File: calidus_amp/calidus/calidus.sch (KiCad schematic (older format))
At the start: 12 parts, among them J1 left_out, J10 service, J11 led_power, J12 sense_bus, J2 power, J3 right_out, J4 left_pot, J5 icsp, J6 input, J7 mute_key, J8 right_pot, J9 led_overload

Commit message: Updated schematic and footprinted Rybicon capacitors
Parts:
- added H1, H2, H3, H4: Mounting, MountingHole:MountingHole_3.2mm_M3_Pad, symbol Mechanical:MountingHole_Pad
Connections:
- no-connect marks 1 -> 5
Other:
- note added: "Mechanical elements"
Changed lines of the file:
@@
 	4700 5100 4700 3900
 Connection ~ 4700 3900
+$Comp
+L Graphic:Logo_Open_Hardware_Small #LOGO1
+U 1 1 5C57F80E
+P 2900 7100
+F 0 "#LOGO1" H 2900 7375 50  0001 C CNN
+F 1 "Logo_Open_Hardware_Small" H 2900 6875 50  0001 C CNN
+F 2 "" H 2900 7100 50  0001 C CNN
+F 3 "~" H 2900 7100 50  0001 C CNN
+	1    2900 7100
+	1    0    0    -1
+$EndComp
+$Comp
+L Mechanical:MountingHole_Pad H1
+U 1 1 5C57F9BC
+P 1200 6900
+F 0 "H1" H 1300 6951 50  0000 L CNN
+F 1 "Mounting" H 1300 6860 50  0000 L CNN
+F 2 "MountingHole:MountingHole_3.2mm_M3_Pad" H 1200 6900 50  0001 C CNN
+F 3 "~" H 1200 6900 50  0001 C CNN
+	1    1200 6900
+	1    0    0    -1
+$EndComp
+NoConn ~ 1200 7000
+$Comp
+L Mechanical:MountingHole_Pad H3
+U 1 1 5C581F06
+P 1200 7200
+F 0 "H3" H 1300 7251 50  0000 L CNN
+F 1 "Mounting" H 1300 7160 50  0000 L CNN
+F 2 "MountingHole:MountingHole_3.2mm_M3_Pad" H 1200 7200 50  0001 C CNN
+F 3 "~" H 1200 7200 50  0001 C CNN
+	1    1200 7200
+	1    0    0    -1
+$EndComp
+NoConn ~ 1200 7300
+$Comp
+L Mechanical:MountingHole_Pad H2
+U 1 1 5C5841CE
+P 1800 6900
+F 0 "H2" H 1900 6951 50  0000 L CNN
+F 1 "Mounting" H 1900 6860 50  0000 L CNN
+F 2 "MountingHole:MountingHole_3.2mm_M3_Pad" H 1800 6900 50  0001 C CNN
+F 3 "~" H 1800 6900 50  0001 C CNN
+	1    1800 6900
+	1    0    0    -1
+$EndComp
+NoConn ~ 1800 7000
+$Comp
+L Mechanical:MountingHole_Pad H4
+U 1 1 5C5841D6
+P 1800 7200
+F 0 "H4" H 1900 7251 50  0000 L CNN
+F 1 "Mounting" H 1900 7160 50  0000 L CNN
+F 2 "MountingHole:MountingHole_3.2mm_M3_Pad" H 1800 7200 50  0001 C CNN
+F 3 "~" H 1800 7200 50  0001 C CNN
+	1    1800 7200
+	1    0    0    -1
+$EndComp
+NoConn ~ 1800 7300
+Wire Notes Line
+	1000 6600 3200 6600
+Wire Notes Line
+	3200 6600 3200 7600
+Wire Notes Line
+	3200 7600 1000 7600
+Wire Notes Line
+	1000 7600 1000 6600
+Text Notes 1100 7500 0    50   ~ 0
+Mechanical elements
 $EndSCHEMATC

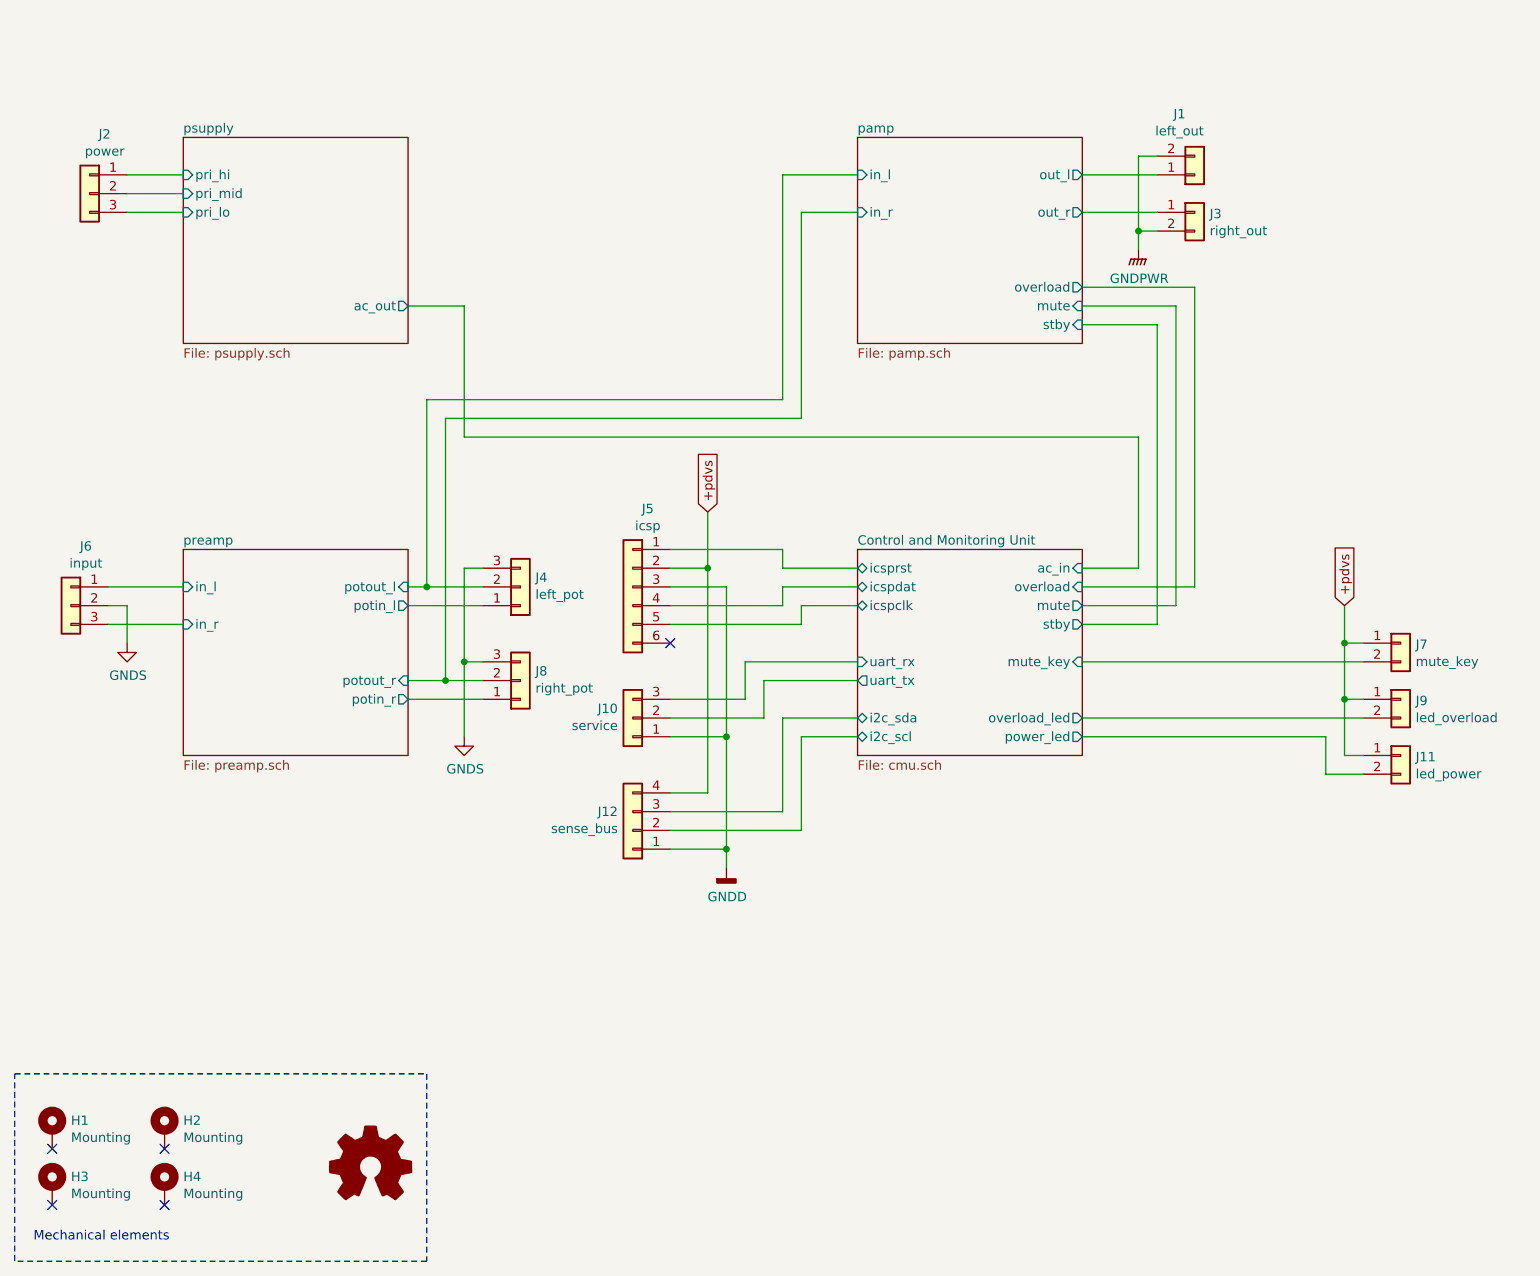
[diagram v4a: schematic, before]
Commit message: WIP: component footprint assignment.
Signed-off-by: Nenad Radulovic <nenad.b.radulovic@gmail.com>
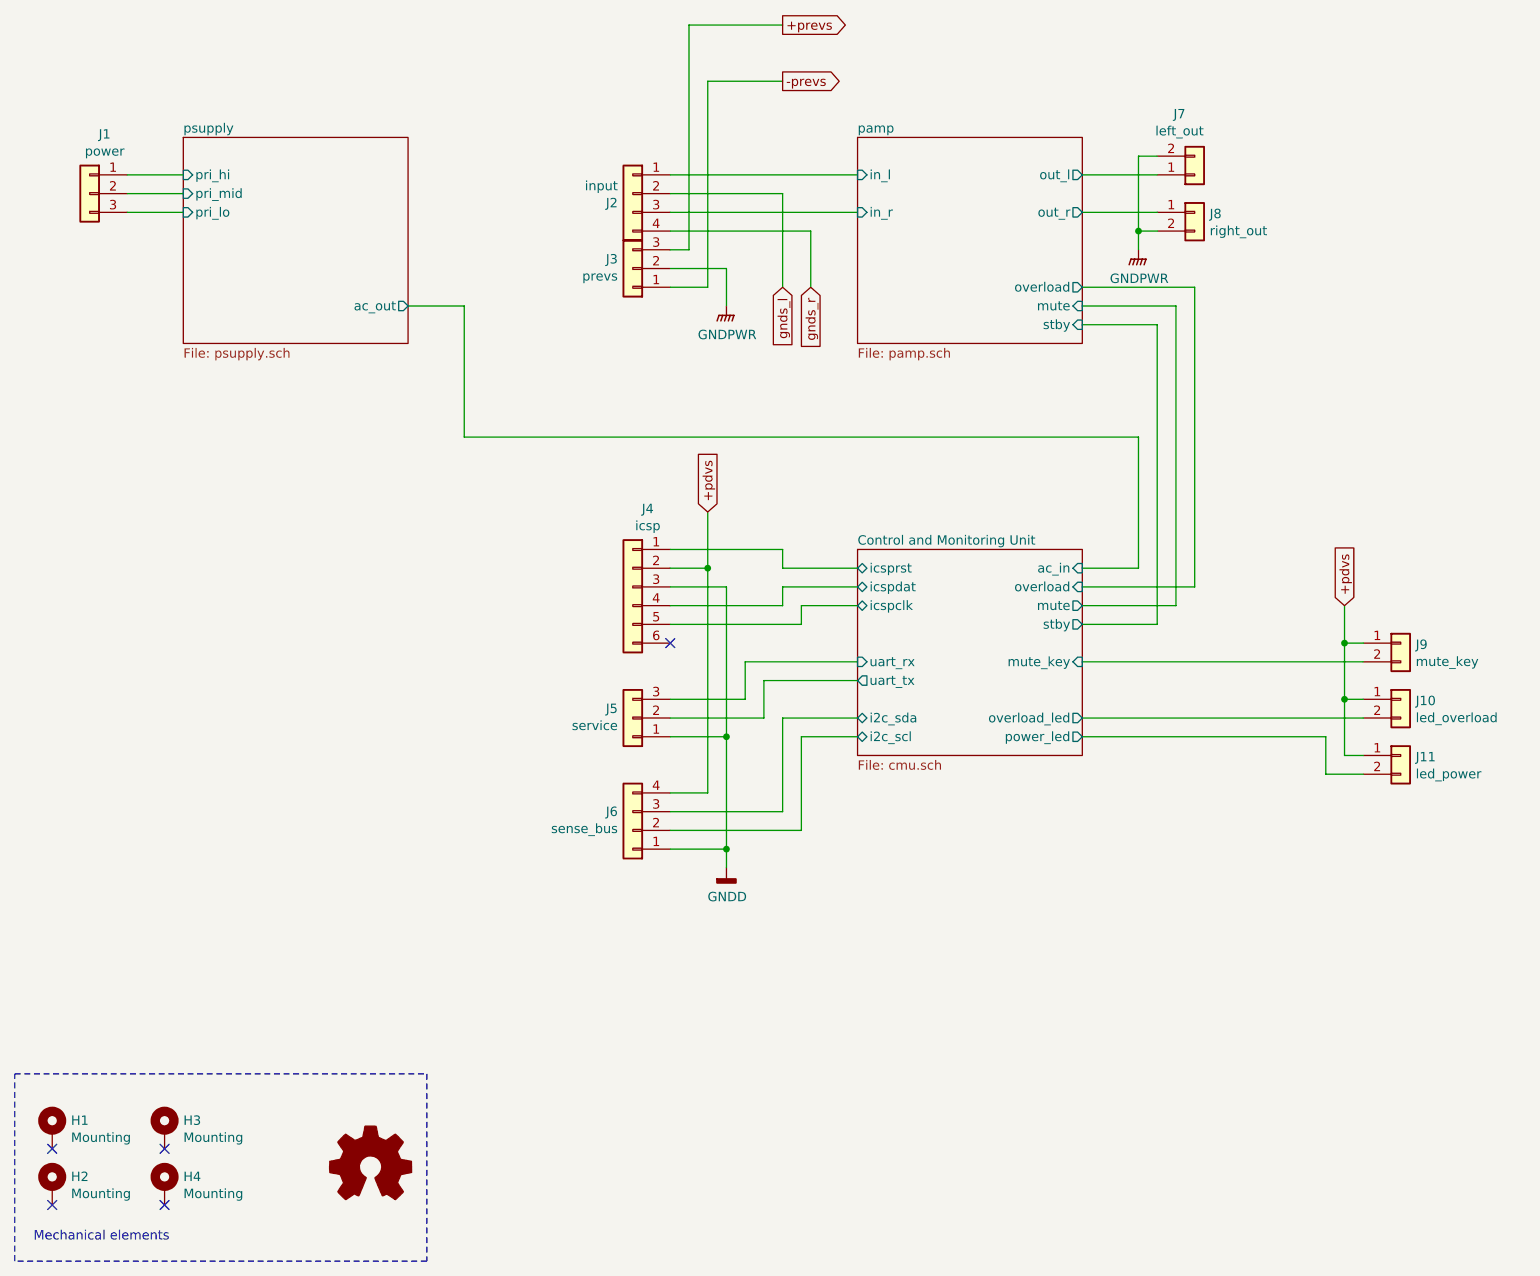
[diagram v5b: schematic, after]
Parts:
- removed J4: left_pot, symbol Connector_Generic:Conn_01x03
- removed J6: input, symbol Connector_Generic:Conn_01x03
- removed J8: right_pot, symbol Connector_Generic:Conn_01x03
- added J2: input, Connector_Phoenix_MC:PhoenixContact_MCV_1,5_3-G-3.5_1x03_P3.50mm_Vertical, symbol Connector_Generic:Conn_01x04
- added J3: prevs, Connector_Phoenix_MC:PhoenixContact_MCV_1,5_3-G-3.5_1x03_P3.50mm_Vertical, symbol Connector_Generic:Conn_01x03
- J1: renamed from J2; footprint (none) -> Connector_Phoenix_MC:PhoenixContact_MCV_1,5_3-G-3.5_1x03_P3.50mm_Vertical
- J7: renamed from J1; footprint (none) -> Connector_Phoenix_MC:PhoenixContact_MCV_1,5_2-G-3.5_1x02_P3.50mm_Vertical
- J8: renamed from J3; footprint (none) -> Connector_Phoenix_MC:PhoenixContact_MCV_1,5_2-G-3.5_1x02_P3.50mm_Vertical
- renumbered H3 to H2, H2 to H3, J9 to J10, J5 to J4, J10 to J5, J12 to J6, J7 to J9
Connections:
- net GNDPWR: now also J3.2 (Pin_2)
- net pamp/in_l: now also J2.1 (Pin_1)
- net pamp/in_r: now also J2.3 (Pin_3)
- new net +prevs: J3.3 (Pin_3)
- new net -prevs: J3.1 (Pin_1)
- new net gnds_l: J2.2 (Pin_2)
- new net gnds_r: J2.4 (Pin_4)
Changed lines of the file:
@@
 $Descr A4 11693 8268
 encoding utf-8
-Sheet 1 5
+Sheet 1 4
 Title ""
 Date ""
@@
 $EndSheet
 $Comp
-L Connector_Generic:Conn_01x03 J2
+L Connector_Generic:Conn_01x03 J1
 U 1 1 5C47FAB8
 P 1400 1900
-F 0 "J2" H 1320 2217 50  0000 C CNN
+F 0 "J1" H 1320 2217 50  0000 C CNN
 F 1 "power" H 1320 2126 50  0000 C CNN
-F 2 "" H 1400 1900 50  0001 C CNN
+F 2 "Connector_Phoenix_MC:PhoenixContact_MCV_1,5_3-G-3.5_1x03_P3.50mm_Vertical" H 1400 1900 50  0001 C CNN
 F 3 "~" H 1400 1900 50  0001 C CNN
 	1    1400 1900
@@
 Wire Wire Line
 	1600 2000 1900 2000
-$Comp
-L Connector_Generic:Conn_01x03 J6
-U 1 1 5C47FB17
-P 1300 4100
-F 0 "J6" H 1220 4417 50  0000 C CNN
-F 1 "input" H 1220 4326 50  0000 C CNN
-F 2 "" H 1300 4100 50  0001 C CNN
-F 3 "~" H 1300 4100 50  0001 C CNN
-	1    1300 4100
-	-1   0    0    -1
-$EndComp
-$Comp
-L power:GNDS #PWR02
-U 1 1 5C47FB54
-P 1600 4300
-F 0 "#PWR02" H 1600 4050 50  0001 C CNN
-F 1 "GNDS" H 1605 4127 50  0000 C CNN
-F 2 "" H 1600 4300 50  0001 C CNN
-F 3 "" H 1600 4300 50  0001 C CNN
-	1    1600 4300
-	1    0    0    -1
-$EndComp
-Wire Wire Line
-	1600 4300 1600 4100
-Wire Wire Line
-	1600 4100 1500 4100
-Wire Wire Line
-	1500 4000 1900 4000
-Wire Wire Line
-	1500 4200 1900 4200
-$Comp
-L Connector_Generic:Conn_01x02 J1
+Wire Wire Line
+	5100 2400 5100 1900
+Wire Wire Line
+	5100 1900 4500 1900
+$Comp
+L Connector_Generic:Conn_01x02 J7
 U 1 1 5C47FBF8
 P 7300 1800
-F 0 "J1" H 7219 1475 50  0000 C CNN
+F 0 "J7" H 7219 1475 50  0000 C CNN
 F 1 "left_out" H 7219 1566 50  0000 C CNN
-F 2 "" H 7300 1800 50  0001 C CNN
+F 2 "Connector_Phoenix_MC:PhoenixContact_MCV_1,5_2-G-3.5_1x02_P3.50mm_Vertical" H 7300 1800 50  0001 C CNN
 F 3 "~" H 7300 1800 50  0001 C CNN
 	1    7300 1800
@@
 $EndComp
 $Comp
-L Connector_Generic:Conn_01x02 J3
+L Connector_Generic:Conn_01x02 J8
 U 1 1 5C47FC30
 P 7300 2000
-F 0 "J3" H 7380 1992 50  0000 L CNN
+F 0 "J8" H 7380 1992 50  0000 L CNN
 F 1 "right_out" H 7380 1901 50  0000 L CNN
-F 2 "" H 7300 2000 50  0001 C CNN
+F 2 "Connector_Phoenix_MC:PhoenixContact_MCV_1,5_2-G-3.5_1x02_P3.50mm_Vertical" H 7300 2000 50  0001 C CNN
 F 3 "~" H 7300 2000 50  0001 C CNN
 	1    7300 2000
@@
 	7000 2100 7100 2100
 $Comp
-L power:GNDPWR #PWR01
+L power:GNDPWR #PWR04
 U 1 1 5C47FEE1
 P 7000 2200
-F 0 "#PWR01" H 7000 2000 50  0001 C CNN
+F 0 "#PWR04" H 7000 2000 50  0001 C CNN
 F 1 "GNDPWR" H 7004 2046 50  0000 C CNN
 F 2 "" H 7000 2150 50  0001 C CNN
@@
 	7000 2200 7000 2100
 Connection ~ 7000 2100
-$Sheet
-S 1900 3800 1200 1100
-U 5C4751C0
-F0 "preamp" 50
-F1 "preamp.sch" 50
-F2 "potout_l" I R 3100 4000 50
-F3 "potin_l" O R 3100 4100 50
-F4 "in_l" I L 1900 4000 50
-F5 "in_r" I L 1900 4200 50
-F6 "potin_r" O R 3100 4600 50
-F7 "potout_r" I R 3100 4500 50
-$EndSheet
-Wire Wire Line
-	3200 3000 5100 3000
-Wire Wire Line
-	5100 3000 5100 1800
-Wire Wire Line
-	5100 1800 5500 1800
-Wire Wire Line
-	3300 3100 5200 3100
-Wire Wire Line
-	5200 3100 5200 2000
-Wire Wire Line
-	5200 2000 5500 2000
-$Comp
-L Connector_Generic:Conn_01x03 J4
-U 1 1 5C438B71
-P 3700 4000
-F 0 "J4" H 3780 3950 50  0000 L CNN
-F 1 "left_pot" H 3780 4041 50  0000 L CNN
-F 2 "" H 3700 4000 50  0001 C CNN
-F 3 "~" H 3700 4000 50  0001 C CNN
-	1    3700 4000
-	1    0    0    1
-$EndComp
-Wire Wire Line
-	3100 4100 3500 4100
-Wire Wire Line
-	3500 4000 3200 4000
-$Comp
-L Connector_Generic:Conn_01x03 J8
-U 1 1 5C4396C1
-P 3700 4500
-F 0 "J8" H 3780 4450 50  0000 L CNN
-F 1 "right_pot" H 3780 4541 50  0000 L CNN
-F 2 "" H 3700 4500 50  0001 C CNN
-F 3 "~" H 3700 4500 50  0001 C CNN
-	1    3700 4500
-	1    0    0    1
-$EndComp
-Wire Wire Line
-	3500 4600 3100 4600
-Wire Wire Line
-	3100 4500 3300 4500
-Wire Wire Line
-	3400 4800 3400 4400
-Wire Wire Line
-	3400 4400 3500 4400
-Wire Wire Line
-	3400 4400 3400 3900
-Wire Wire Line
-	3400 3900 3500 3900
-Connection ~ 3400 4400
-$Comp
-L power:GNDS #PWR03
-U 1 1 5C43A2D2
-P 3400 4800
-F 0 "#PWR03" H 3400 4550 50  0001 C CNN
-F 1 "GNDS" H 3405 4627 50  0000 C CNN
-F 2 "" H 3400 4800 50  0001 C CNN
-F 3 "" H 3400 4800 50  0001 C CNN
-	1    3400 4800
-	1    0    0    -1
-$EndComp
+Wire Wire Line
+	4500 1800 5500 1800
+Wire Wire Line
+	4500 2000 5500 2000
 Wire Wire Line
 	6700 2600 7100 2600
@@
 Wire Wire Line
 	7300 4000 6700 4000
-Wire Wire Line
-	3200 3000 3200 4000
-Connection ~ 3200 4000
-Wire Wire Line
-	3200 4000 3100 4000
-Wire Wire Line
-	3300 3100 3300 4500
-Connection ~ 3300 4500
-Wire Wire Line
-	3300 4500 3500 4500
 Wire Wire Line
 	3100 2500 3400 2500
@@
 +pdvs
 $Comp
-L Connector_Generic:Conn_01x02 J9
+L Connector_Generic:Conn_01x02 J10
 U 1 1 5C4DAFE8
 P 8400 4600
-F 0 "J9" H 8480 4592 50  0000 L CNN
+F 0 "J10" H 8480 4592 50  0000 L CNN
 F 1 "led_overload" H 8480 4501 50  0000 L CNN
 F 2 "Connector_PinHeader_2.54mm:PinHeader_1x02_P2.54mm_Vertical" H 8400 4600 50  0001 C CNN
@@
 Connection ~ 8100 4600
 $Comp
-L Connector_Generic:Conn_01x02 J7
+L Connector_Generic:Conn_01x02 J9
 U 1 1 5C4E1437
 P 8400 4300
-F 0 "J7" H 8480 4292 50  0000 L CNN
+F 0 "J9" H 8480 4292 50  0000 L CNN
 F 1 "mute_key" H 8480 4201 50  0000 L CNN
 F 2 "Connector_PinHeader_2.54mm:PinHeader_1x02_P2.54mm_Vertical" H 8400 4300 50  0001 C CNN
@@
 	7000 3900 6700 3900
 $Comp
-L Connector_Generic:Conn_01x06 J5
+L Connector_Generic:Conn_01x06 J4
 U 1 1 5C4F09AA
 P 4300 4000
-F 0 "J5" H 4220 4417 50  0000 C CNN
+F 0 "J4" H 4220 4417 50  0000 C CNN
 F 1 "icsp" H 4220 4326 50  0000 C CNN
 F 2 "Connector_PinHeader_2.54mm:PinHeader_1x06_P2.54mm_Vertical" H 4300 4000 50  0001 C CNN
@@
 P 4800 5500
 AR Path="/5C43C4AB/5C504FC8" Ref="#PWR?"  Part="1"
-AR Path="/5C504FC8" Ref="#PWR04"  Part="1"
-F 0 "#PWR04" H 4800 5250 50  0001 C CNN
+AR Path="/5C504FC8" Ref="#PWR02"  Part="1"
+F 0 "#PWR02" H 4800 5250 50  0001 C CNN
 F 1 "GNDD" H 4804 5345 50  0000 C CNN
 F 2 "" H 4800 5500 50  0001 C CNN
@@
 	4500 4200 5200 4200
 $Comp
-L Connector_Generic:Conn_01x03 J10
+L Connector_Generic:Conn_01x03 J5
 U 1 1 5C51607F
 P 4300 4700
-F 0 "J10" H 4380 4650 50  0000 L CNN
+F 0 "J5" H 4380 4650 50  0000 L CNN
 F 1 "service" H 4380 4741 50  0000 L CNN
 F 2 "Connector_PinHeader_2.54mm:PinHeader_1x03_P2.54mm_Vertical" H 4300 4700 50  0001 C CNN
@@
 	4800 4000 4500 4000
 $Comp
-L Connector_Generic:Conn_01x04 J12
+L Connector_Generic:Conn_01x04 J6
 U 1 1 5C5CE216
 P 4300 5300
-F 0 "J12" H 4380 5200 50  0000 L CNN
+F 0 "J6" H 4380 5200 50  0000 L CNN
 F 1 "sense_bus" H 4380 5291 50  0000 L CNN
 F 2 "Connector_PinHeader_2.54mm:PinHeader_1x04_P2.54mm_Vertical" H 4300 5300 50  0001 C CNN
@@
 NoConn ~ 1200 7000
 $Comp
-L Mechanical:MountingHole_Pad H3
+L Mechanical:MountingHole_Pad H2
 U 1 1 5C581F06
 P 1200 7200
-F 0 "H3" H 1300 7251 50  0000 L CNN
+F 0 "H2" H 1300 7251 50  0000 L CNN
 F 1 "Mounting" H 1300 7160 50  0000 L CNN
 F 2 "MountingHole:MountingHole_3.2mm_M3_Pad" H 1200 7200 50  0001 C CNN
@@
 NoConn ~ 1200 7300
 $Comp
-L Mechanical:MountingHole_Pad H2
+L Mechanical:MountingHole_Pad H3
 U 1 1 5C5841CE
 P 1800 6900
-F 0 "H2" H 1900 6951 50  0000 L CNN
+F 0 "H3" H 1900 6951 50  0000 L CNN
 F 1 "Mounting" H 1900 6860 50  0000 L CNN
 F 2 "MountingHole:MountingHole_3.2mm_M3_Pad" H 1800 6900 50  0001 C CNN
@@
 Text Notes 1100 7500 0    50   ~ 0
 Mechanical elements
+$Comp
+L power:GNDPWR #PWR01
+U 1 1 5C50E81E
+P 4800 2500
+F 0 "#PWR01" H 4800 2300 50  0001 C CNN
+F 1 "GNDPWR" H 4804 2346 50  0000 C CNN
+F 2 "" H 4800 2450 50  0001 C CNN
+F 3 "" H 4800 2450 50  0001 C CNN
+	1    4800 2500
+	1    0    0    -1
+$EndComp
+Wire Wire Line
+	4800 2500 4800 2300
+Wire Wire Line
+	4800 2300 4500 2300
+Text GLabel 5100 1000 2    50   Output ~ 0
++prevs
+Text GLabel 5100 1300 2    50   Output ~ 0
+-prevs
+Wire Wire Line
+	4500 2200 4600 2200
+Wire Wire Line
+	4600 2200 4600 1000
+Wire Wire Line
+	4500 2400 4700 2400
+Wire Wire Line
+	4700 2400 4700 1300
+Wire Wire Line
+	4700 1300 5100 1300
+Wire Wire Line
+	4600 1000 5100 1000
+$Comp
+L Connector_Generic:Conn_01x04 J2
+U 1 1 5C540E50
+P 4300 1900
+F 0 "J2" H 4380 1850 50  0000 L CNN
+F 1 "input" H 4380 1941 50  0000 L CNN
+F 2 "Connector_Phoenix_MC:PhoenixContact_MCV_1,5_3-G-3.5_1x03_P3.50mm_Vertical" H 4300 1900 50  0001 C CNN
+F 3 "~" H 4300 1900 50  0001 C CNN
+	1    4300 1900
+	-1   0    0    -1
+$EndComp
+$Comp
+L Connector_Generic:Conn_01x03 J3
+U 1 1 5C540ED0
+P 4300 2300
+F 0 "J3" H 4380 2250 50  0000 L CNN
+F 1 "prevs" H 4380 2341 50  0000 L CNN
+F 2 "Connector_Phoenix_MC:PhoenixContact_MCV_1,5_3-G-3.5_1x03_P3.50mm_Vertical" H 4300 2300 50  0001 C CNN
+F 3 "~" H 4300 2300 50  0001 C CNN
+	1    4300 2300
+	-1   0    0    1
+$EndComp
+Text GLabel 5100 2400 3    50   Input ~ 0
+gnds_l
+Text GLabel 5250 2400 3    50   Input ~ 0
+gnds_r
+Wire Wire Line
+	5250 2400 5250 2100
+Wire Wire Line
+	5250 2100 4500 2100
 $EndSCHEMATC
